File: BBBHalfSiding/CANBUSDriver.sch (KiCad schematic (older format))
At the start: 13 parts, among them J2 RJ45, J3 RJ45, P10 + 12 out -, P6 Termination, P7 + 12 in -, U11 74LV125AN, U12 MCP2551

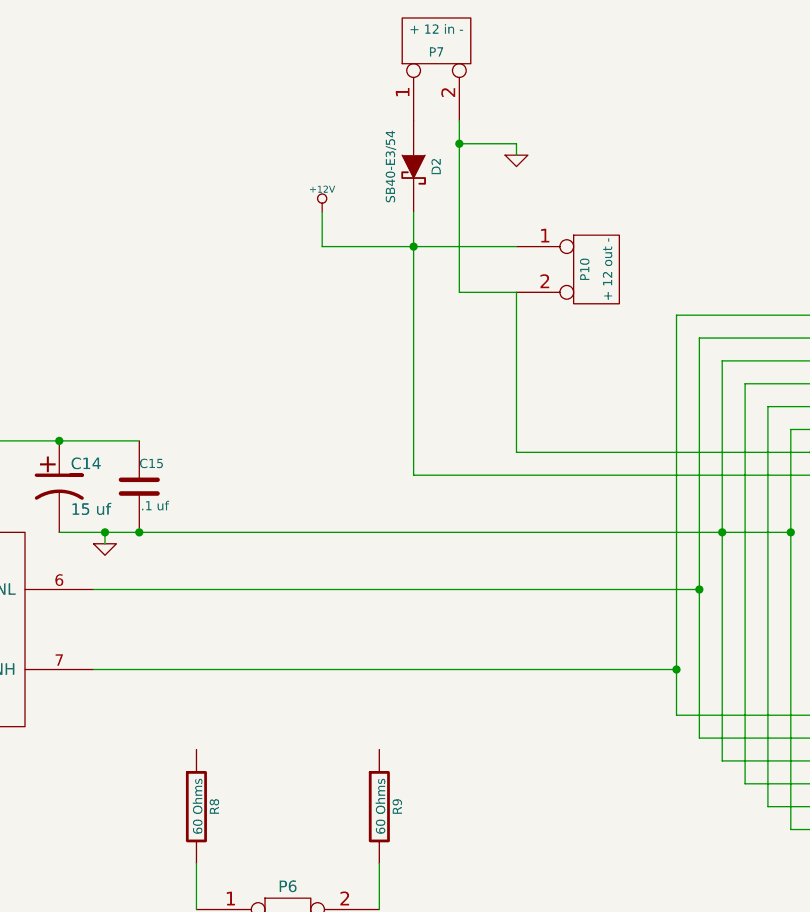
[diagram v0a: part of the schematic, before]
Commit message: Completed Beagle Bone Black Half Siding Cape
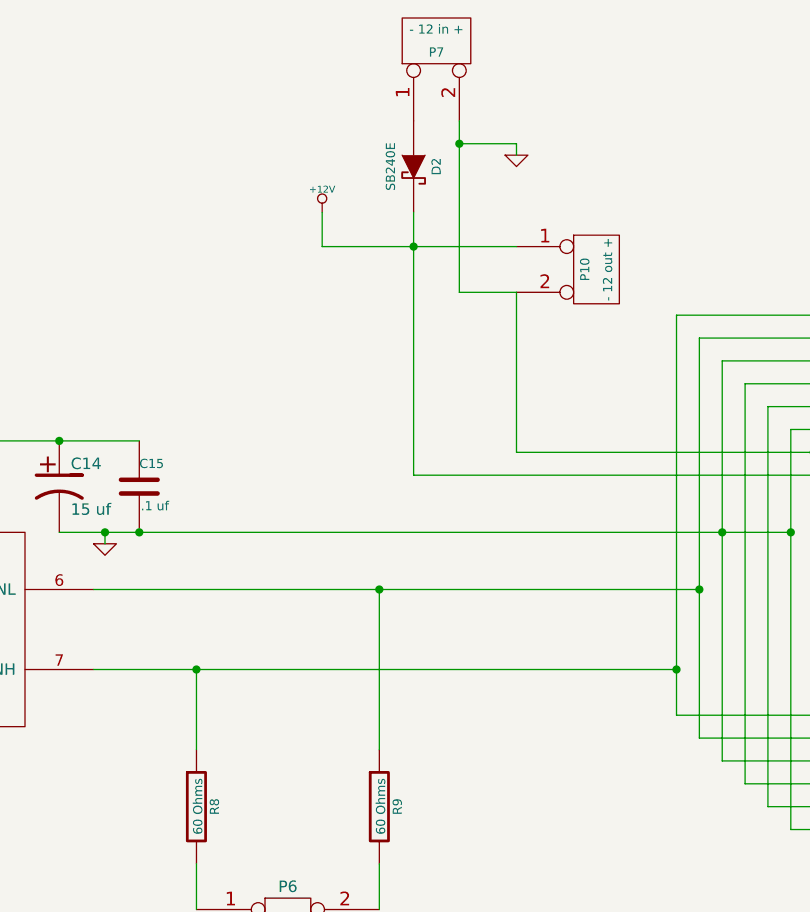
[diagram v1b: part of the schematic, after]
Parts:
- C14: Mouser Part Number (none) -> 98-156CKR050M
- D2: value SB40-E3/54 -> SB240E; Mouser Part Number (none) -> 625-SB240-E3/73
- P10: value + 12 out - -> - 12 out +
- P7: value + 12 in - -> - 12 in +
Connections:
- net at J2.2, J3.2, U12.6 (CANL): now also R9.1
- net at J2.1, J3.1, U12.7 (CANH): now also R8.1
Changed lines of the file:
@@
 LIBS:mcp25xxx
 LIBS:74lv125AN
+LIBS:cat24c256w
 LIBS:BBBHalfSiding-cache
 EELAYER 27 0
@@
 Sheet 4 4
 Title ""
-Date "18 oct 2018"
+Date "19 oct 2018"
 Rev ""
 Comp ""
@@
 $EndComp
 $Comp
-L GND #PWR052
+L GND #PWR055
 U 1 1 5BC8C35C
 P 3900 3500
-F 0 "#PWR052" H 3900 3500 30  0001 C CNN
+F 0 "#PWR055" H 3900 3500 30  0001 C CNN
 F 1 "GND" H 3900 3430 30  0001 C CNN
 F 2 "" H 3900 3500 60  0000 C CNN
@@
 Connection ~ 3900 3450
 $Comp
-L +5V #PWR053
+L +5V #PWR056
 U 1 1 5BC8C37B
 P 5250 2300
-F 0 "#PWR053" H 5250 2390 20  0001 C CNN
+F 0 "#PWR056" H 5250 2390 20  0001 C CNN
 F 1 "+5V" H 5250 2390 30  0000 C CNN
 F 2 "" H 5250 2300 60  0000 C CNN
@@
 $EndComp
 $Comp
-L +3.3V #PWR054
+L +3.3V #PWR057
 U 1 1 5BC8C9AA
 P 3900 3000
-F 0 "#PWR054" H 3900 2960 30  0001 C CNN
+F 0 "#PWR057" H 3900 2960 30  0001 C CNN
 F 1 "+3.3V" H 3900 3110 30  0000 C CNN
 F 2 "" H 3900 3000 60  0000 C CNN
@@
 	4600 4000 5250 4000
 $Comp
-L GND #PWR055
+L GND #PWR058
 U 1 1 5BC8C9E6
 P 5250 4150
-F 0 "#PWR055" H 5250 4150 30  0001 C CNN
+F 0 "#PWR058" H 5250 4150 30  0001 C CNN
 F 1 "GND" H 5250 4080 30  0001 C CNN
 F 2 "" H 5250 4150 60  0000 C CNN
@@
 F 2 "~" H 5750 2650 60  0000 C CNN
 F 3 "~" H 5750 2650 60  0000 C CNN
+F 4 "98-156CKR050M" H 5750 2650 60  0001 C CNN "Mouser Part Number"
 	1    5750 2650
 	1    0    0    -1
@@
 Connection ~ 5750 2450
 $Comp
-L GND #PWR056
+L GND #PWR059
 U 1 1 5BC8CA74
 P 5950 2900
-F 0 "#PWR056" H 5950 2900 30  0001 C CNN
+F 0 "#PWR059" H 5950 2900 30  0001 C CNN
 F 1 "GND" H 5950 2830 30  0001 C CNN
 F 2 "" H 5950 2900 60  0000 C CNN
@@
 $EndComp
 $Comp
-L GND #PWR057
+L GND #PWR060
 U 1 1 5BC8CB07
 P 6850 5500
-F 0 "#PWR057" H 6850 5500 30  0001 C CNN
+F 0 "#PWR060" H 6850 5500 30  0001 C CNN
 F 1 "GND" H 6850 5430 30  0001 C CNN
 F 2 "" H 6850 5500 60  0000 C CNN
@@
 P 7400 700
 F 0 "P7" V 7350 700 40  0000 C CNN
-F 1 "+ 12 in -" V 7450 700 40  0000 C CNN
+F 1 "- 12 in +" V 7450 700 40  0000 C CNN
 F 2 "" H 7400 700 60  0000 C CNN
 F 3 "" H 7400 700 60  0000 C CNN
@@
 P 8100 1700
 F 0 "P10" V 8050 1700 40  0000 C CNN
-F 1 "+ 12 out -" V 8150 1700 40  0000 C CNN
+F 1 "- 12 out +" V 8150 1700 40  0000 C CNN
 F 2 "" H 8100 1700 60  0000 C CNN
 F 3 "" H 8100 1700 60  0000 C CNN
@@
 P 7300 1250
 F 0 "D2" H 7300 1350 40  0000 C CNN
-F 1 "SB40-E3/54" H 7300 1150 40  0000 C CNN
+F 1 "SB240E" H 7300 1150 40  0000 C CNN
 F 2 "~" H 7300 1250 60  0000 C CNN
 F 3 "~" H 7300 1250 60  0000 C CNN
+F 4 "625-SB240-E3/73" H 7300 1250 60  0001 C CNN "Mouser Part Number"
 	1    7300 1250
 	0    1    1    0
@@
 	7500 1800 7500 1050
 $Comp
-L +12V #PWR058
+L +12V #PWR061
 U 1 1 5BC8D996
 P 6900 1450
-F 0 "#PWR058" H 6900 1400 20  0001 C CNN
+F 0 "#PWR061" H 6900 1400 20  0001 C CNN
 F 1 "+12V" H 6900 1550 30  0000 C CNN
 F 2 "" H 6900 1450 60  0000 C CNN
@@
 	6900 1450 6900 1600
 $Comp
-L GND #PWR059
+L GND #PWR062
 U 1 1 5BC8D9F0
 P 7750 1200
-F 0 "#PWR059" H 7750 1200 30  0001 C CNN
+F 0 "#PWR062" H 7750 1200 30  0001 C CNN
 F 1 "GND" H 7750 1130 30  0001 C CNN
 F 2 "" H 7750 1200 60  0000 C CNN
@@
 	7750 1150 7500 1150
 Connection ~ 7500 1150
+Wire Wire Line
+	7150 3800 7150 3100
+Connection ~ 7150 3100
+Wire Wire Line
+	6350 3800 6350 3450
+Connection ~ 6350 3450
 $EndSCHEMATC

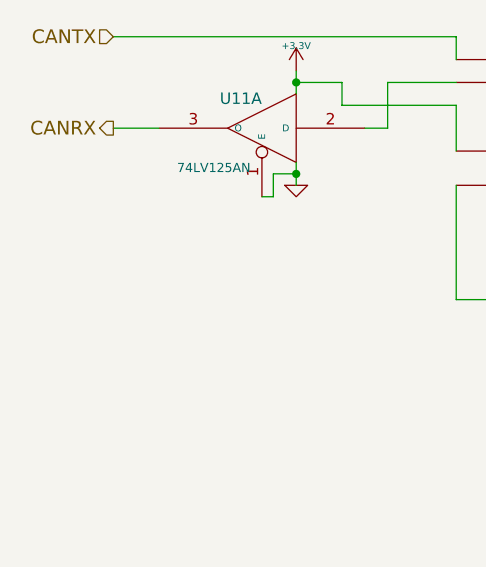
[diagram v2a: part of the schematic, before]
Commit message: Add missing bypass caps.
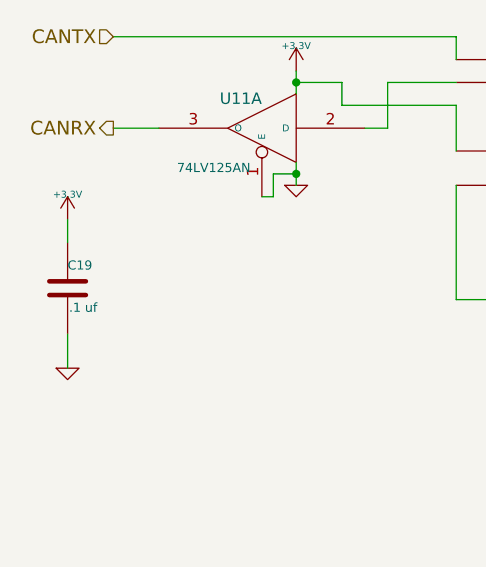
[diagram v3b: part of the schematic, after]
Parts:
- added C19: .1 uf, ~, symbol C
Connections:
- net +3V3: now also C19.1
- net GND: now also C19.2
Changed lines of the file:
@@
 $EndComp
 $Comp
-L GND #PWR055
+L GND #PWR057
 U 1 1 5BC8C35C
 P 3900 3500
-F 0 "#PWR055" H 3900 3500 30  0001 C CNN
+F 0 "#PWR057" H 3900 3500 30  0001 C CNN
 F 1 "GND" H 3900 3430 30  0001 C CNN
 F 2 "" H 3900 3500 60  0000 C CNN
@@
 Connection ~ 3900 3450
 $Comp
-L +5V #PWR056
+L +5V #PWR058
 U 1 1 5BC8C37B
 P 5250 2300
-F 0 "#PWR056" H 5250 2390 20  0001 C CNN
+F 0 "#PWR058" H 5250 2390 20  0001 C CNN
 F 1 "+5V" H 5250 2390 30  0000 C CNN
 F 2 "" H 5250 2300 60  0000 C CNN
@@
 $EndComp
 $Comp
-L +3.3V #PWR057
+L +3.3V #PWR059
 U 1 1 5BC8C9AA
 P 3900 3000
-F 0 "#PWR057" H 3900 2960 30  0001 C CNN
+F 0 "#PWR059" H 3900 2960 30  0001 C CNN
 F 1 "+3.3V" H 3900 3110 30  0000 C CNN
 F 2 "" H 3900 3000 60  0000 C CNN
@@
 	4600 4000 5250 4000
 $Comp
-L GND #PWR058
+L GND #PWR060
 U 1 1 5BC8C9E6
 P 5250 4150
-F 0 "#PWR058" H 5250 4150 30  0001 C CNN
+F 0 "#PWR060" H 5250 4150 30  0001 C CNN
 F 1 "GND" H 5250 4080 30  0001 C CNN
 F 2 "" H 5250 4150 60  0000 C CNN
@@
 Connection ~ 5750 2450
 $Comp
-L GND #PWR059
+L GND #PWR061
 U 1 1 5BC8CA74
 P 5950 2900
-F 0 "#PWR059" H 5950 2900 30  0001 C CNN
+F 0 "#PWR061" H 5950 2900 30  0001 C CNN
 F 1 "GND" H 5950 2830 30  0001 C CNN
 F 2 "" H 5950 2900 60  0000 C CNN
@@
 $EndComp
 $Comp
-L GND #PWR060
+L GND #PWR062
 U 1 1 5BC8CB07
 P 6850 5500
-F 0 "#PWR060" H 6850 5500 30  0001 C CNN
+F 0 "#PWR062" H 6850 5500 30  0001 C CNN
 F 1 "GND" H 6850 5430 30  0001 C CNN
 F 2 "" H 6850 5500 60  0000 C CNN
@@
 	7500 1800 7500 1050
 $Comp
-L +12V #PWR061
+L +12V #PWR063
 U 1 1 5BC8D996
 P 6900 1450
-F 0 "#PWR061" H 6900 1400 20  0001 C CNN
+F 0 "#PWR063" H 6900 1400 20  0001 C CNN
 F 1 "+12V" H 6900 1550 30  0000 C CNN
 F 2 "" H 6900 1450 60  0000 C CNN
@@
 	6900 1450 6900 1600
 $Comp
-L GND #PWR062
+L GND #PWR064
 U 1 1 5BC8D9F0
 P 7750 1200
-F 0 "#PWR062" H 7750 1200 30  0001 C CNN
+F 0 "#PWR064" H 7750 1200 30  0001 C CNN
 F 1 "GND" H 7750 1130 30  0001 C CNN
 F 2 "" H 7750 1200 60  0000 C CNN
@@
 	6350 3800 6350 3450
 Connection ~ 6350 3450
+$Comp
+L C C19
+U 1 1 5BCB5272
+P 2900 3950
+F 0 "C19" H 2900 4050 40  0000 L CNN
+F 1 ".1 uf" H 2906 3865 40  0000 L CNN
+F 2 "~" H 2938 3800 30  0000 C CNN
+F 3 "~" H 2900 3950 60  0000 C CNN
+	1    2900 3950
+	1    0    0    -1
+$EndComp
+$Comp
+L +3.3V #PWR065
+U 1 1 5BCB52DB
+P 2900 3650
+F 0 "#PWR065" H 2900 3610 30  0001 C CNN
+F 1 "+3.3V" H 2900 3760 30  0000 C CNN
+F 2 "" H 2900 3650 60  0000 C CNN
+F 3 "" H 2900 3650 60  0000 C CNN
+	1    2900 3650
+	1    0    0    -1
+$EndComp
+$Comp
+L GND #PWR066
+U 1 1 5BCB52EA
+P 2900 4300
+F 0 "#PWR066" H 2900 4300 30  0001 C CNN
+F 1 "GND" H 2900 4230 30  0001 C CNN
+F 2 "" H 2900 4300 60  0000 C CNN
+F 3 "" H 2900 4300 60  0000 C CNN
+	1    2900 4300
+	1    0    0    -1
+$EndComp
+Wire Wire Line
+	2900 3650 2900 3750
+Wire Wire Line
+	2900 4150 2900 4300
 $EndSCHEMATC

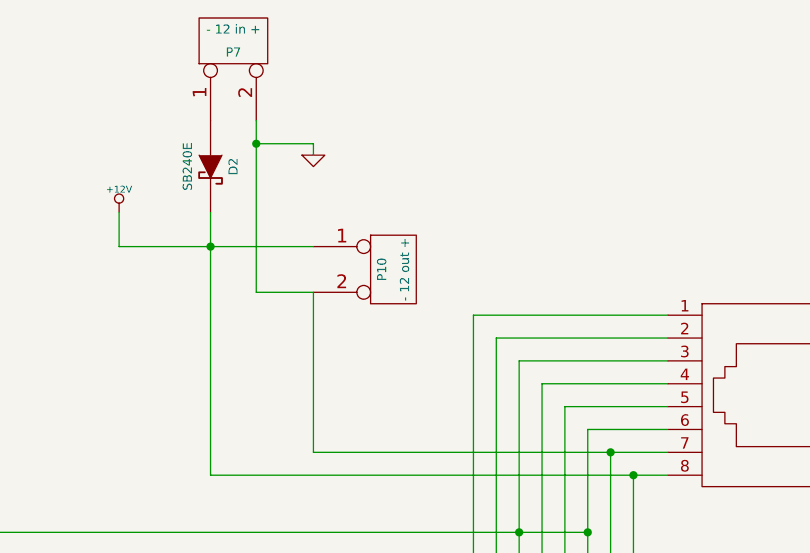
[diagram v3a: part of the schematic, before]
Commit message: Tweaks to the silk screen for BBBHalfSiding cape.
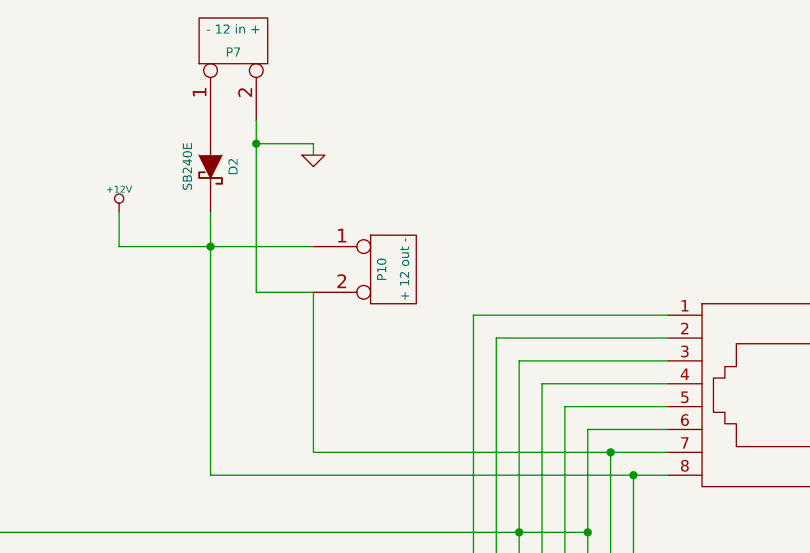
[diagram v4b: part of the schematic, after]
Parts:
- P10: value - 12 out + -> + 12 out -
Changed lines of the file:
@@
 P 8100 1700
 F 0 "P10" V 8050 1700 40  0000 C CNN
-F 1 "- 12 out +" V 8150 1700 40  0000 C CNN
+F 1 "+ 12 out -" V 8150 1700 40  0000 C CNN
 F 2 "" H 8100 1700 60  0000 C CNN
 F 3 "" H 8100 1700 60  0000 C CNN
